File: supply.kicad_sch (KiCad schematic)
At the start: 84 parts, among them IC901 TPS7A0518PDBVT, J3 PJ-102A, Q1 BCM857BS-7-F, Q2 BCM857BS-7-F, Q3 SSM3J332R, Q4 SSM3J332R, Q901 BSS138W-7-F, Q902 BSS138W-7-F, Q903 BSS138W-7-F, SW901 PCM12SMTR, U3 TPS7B8133DRVR, U901 RB521S30T1G, U902 RB521S30T1G, U903 MP2386GG-P, U904 MP2386GG-P, U905 74LVC2G14GV, U906 74LVC1G175GV

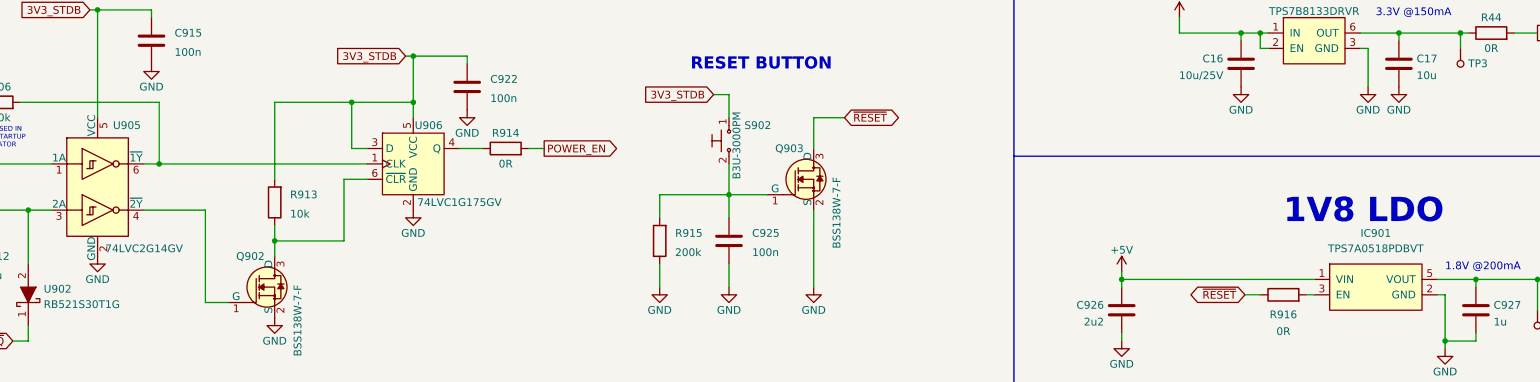
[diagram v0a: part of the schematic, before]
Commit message: SCH: Cosmetic improvement & unification
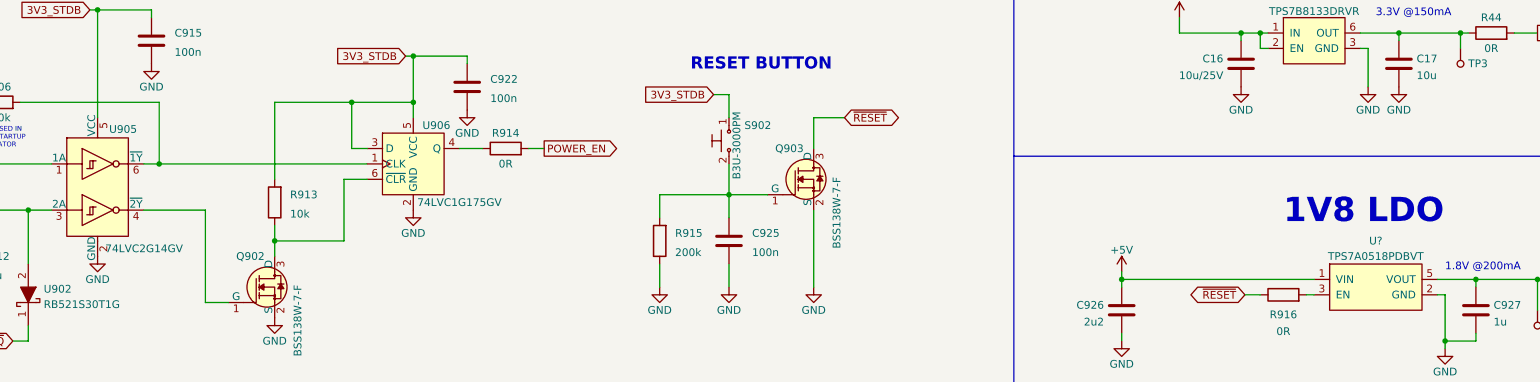
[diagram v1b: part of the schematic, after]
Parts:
- renumbered IC901 to U?
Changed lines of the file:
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@@
   (symbol (lib_id "antmicroLogicBuffersDriversReceiversTransceivers:74LVC2G14GV") (at 138.43 54.61 0) (unit 1)
     (in_bom yes) (on_board yes)
-    (property "Reference" "U905" (id 0) (at 140.97 45.72 0)
+    (property "Reference" "U905" (id 0) (at 140.335 46.355 0)
       (effects (font (size 1.27 1.27)) (justify left))
     )
@@
   (symbol (lib_id "antmicroLogicGatesandInverters:74LVC1G175GV") (at 190.5 52.07 0) (unit 1)
     (in_bom yes) (on_board yes)
-    (property "Reference" "U906" (id 0) (at 193.04 45.72 0))
+    (property "Reference" "U906" (id 0) (at 194.31 45.72 0))
     (property "Value" "74LVC1G175GV" (id 1) (at 198.12 58.42 0))
     (property "Footprint" "antmicro-footprints:SOT-23-6" (id 2) (at 190.5 69.85 0)
@@
   )
   (symbol (lib_id "antmicroPMICVoltageRegulatorsLinear:TPS7A0518PDBVT") (at 349.25 72.39 0) (unit 1)
-    (in_bom yes) (on_board yes) (fields_autoplaced)
-    (property "Reference" "IC901" (id 0) (at 349.25 63.5 0))
-    (property "Value" "TPS7A0518PDBVT" (id 1) (at 349.25 66.04 0))
+    (in_bom yes) (on_board yes)
+    (property "Reference" "U?" (id 0) (at 349.25 64.77 0))
+    (property "Value" "TPS7A0518PDBVT" (id 1) (at 349.25 67.31 0))
     (property "Footprint" "antmicro-footprints:SOT-23-5" (id 2) (at 349.25 78.74 0)
       (effects (font (size 1.27 1.27)) hide)

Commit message: Add 3V3 rail discharge
- add 3V3 rail discharge circuitry
- add 3V3 and 5V0 switch side labels
- minor improvements in arrangement on the supply sheet
- minor update on m-2 sheet
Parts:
- added Q? (x2): DMG1012T-7, antmicro-footprints:SOT-523, symbol antmicroTransistorsFETsMOSFETsSingle:DMG1012T-7
- added R?: R_100k_0402, antmicro-footprints:0402-res, symbol antmicroResistors0402:R_100k_0402
- added R?: R_5R6_0402, antmicro-footprints:0402-res, symbol antmicroResistors0402:R_5R6_0402
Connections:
- net +5V: now also R?.2
- net 3V3_EN: now also Q?.1 (G)
- net GND: now also Q?.2 (S), Q?.2 (S)
- net 3V3_SW: now reaches L902.1 (P), U904.6 (SW)
- net 3V3_SW: now also C914.2; no longer C914.1
- net 3V3_BST: now reaches U904.7 (BST)
- net 3V3_BST: now also C914.1; no longer C914.2
- net 1V8_LDO: now reaches C927.1, R45.1, TP907.1, U?.5 (VOUT)
- net 5V0_SW: now reaches C913.1, L901.1 (P), U903.6 (SW)
- net 5V0_BST: now reaches C913.2, U903.7 (BST)
- net 3V3_REG: now reaches C917.1, C919.1, C921.1, C924.1, L902.2 (P), R47.1, R911.2, TP4.1
- net 3V3_REG: now also R?.2
- net 5V0_REG: now reaches C916.1, C918.1, C920.1, C923.1, L901.2 (P), R46.1, R909.2, TP905.1
- net 3V3_LDO: now reaches C17.1, R44.1, TP3.1, U3.6 (OUT)
- new net: Q?.1 (G), Q?.3 (D), R?.1
- new net: Q?.3 (D), R?.1
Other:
- note added: "3V3 rail discharge"
- moved on the sheet: C901, C902, C904, C905, C906, C907, C908, C909, C910, C911, C913, C914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

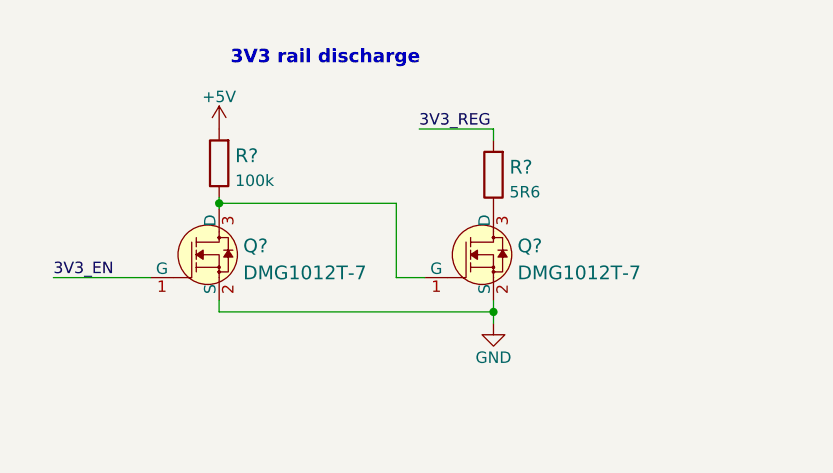
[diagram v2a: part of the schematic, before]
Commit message: Changed discharge MOSFETs to unify components used
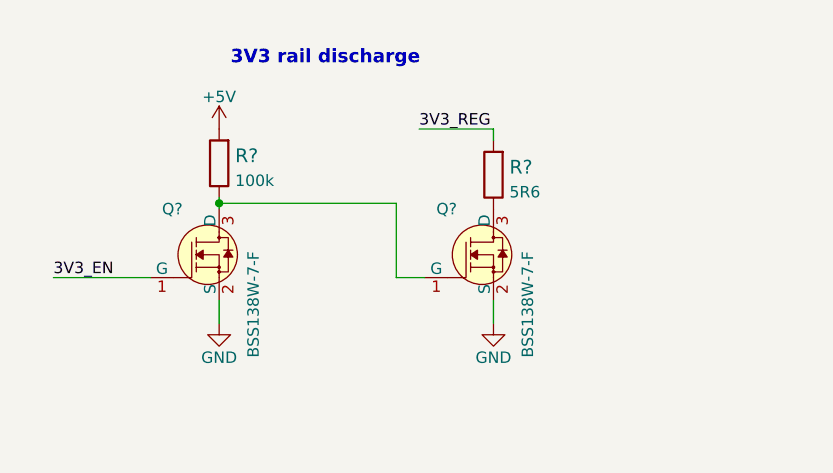
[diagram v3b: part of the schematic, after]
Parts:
- removed Q? (x2): DMG1012T-7, antmicro-footprints:SOT-523, symbol antmicroTransistorsFETsMOSFETsSingle:DMG1012T-7
- added Q? (x2): BSS138W-7-F, antmicro-footprints:SOT-323, symbol antmicroTransistorsFETsMOSFETsSingle:BSS138W-7-F
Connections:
- net 3V3_EN: now also Q?.1 (G)
- net GND: now also Q?.2 (S), Q?.2 (S)
- net at R?.1: now also Q?.1 (G), Q?.3 (D)
- net at R?.1: now also Q?.3 (D)
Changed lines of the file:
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@@
   (junction (at 353.06 127) (diameter 0) (color 0 0 0 0)
   )
-  (junction (at 279.4 267.97) (diameter 0) (color 0 0 0 0)
-  )
   (junction (at 249.555 127) (diameter 0) (color 0 0 0 0)
   )
@@
     (stroke (width 0) (type default) (color 0 0 0 0))
   )
-  (wire (pts (xy 279.4 266.7) (xy 279.4 267.97))
+  (wire (pts (xy 279.4 266.7) (xy 279.4 269.24))
     (stroke (width 0) (type default) (color 0 0 0 0))
   )
@@
     (stroke (width 0) (type default) (color 0 0 0 0))
   )
-  (wire (pts (xy 279.4 267.97) (xy 248.92 267.97))
-    (stroke (width 0) (type default) (color 0 0 0 0))
-  )
   (wire (pts (xy 339.725 127) (xy 353.06 127))
     (stroke (width 0) (type default) (color 0 0 0 0))
@@
     (stroke (width 0) (type default) (color 0 0 0 0))
   )
-  (wire (pts (xy 248.92 267.97) (xy 248.92 266.7))
-    (stroke (width 0) (type default) (color 0 0 0 0))
-  )
   (wire (pts (xy 374.015 208.28) (xy 374.015 209.55))
     (stroke (width 0) (type default) (color 0 0 0 0))
@@
     (stroke (width 0) (type default) (color 0 0 0 0))
   )
-  (wire (pts (xy 279.4 267.97) (xy 279.4 269.24))
-    (stroke (width 0) (type default) (color 0 0 0 0))
-  )
   (polyline (pts (xy 12.7 252.73) (xy 219.075 252.73))
     (stroke (width 0) (type default) (color 0 0 0 0))
@@
     (stroke (width 0) (type default) (color 0 0 0 0))
   )
+  (wire (pts (xy 248.92 266.7) (xy 248.92 269.24))
+    (stroke (width 0) (type default) (color 0 0 0 0))
+  )
   (wire (pts (xy 50.8 52.07) (xy 50.8 66.04))
     (stroke (width 0) (type default) (color 0 0 0 0))
@@
     (pin "1")
   )
-  (symbol (lib_id "antmicroTransistorsFETsMOSFETsSingle:DMG1012T-7") (at 248.92 261.62 0) (unit 1)
-    (in_bom yes) (on_board yes) (fields_autoplaced)
-    (property "Reference" "Q?" (id 0) (at 251.587 260.6438 0)
-      (effects (font (size 1.524 1.524)) (justify left))
-    )
-    (property "Value" "DMG1012T-7" (id 1) (at 251.587 263.6372 0)
-      (effects (font (size 1.524 1.524)) (justify left))
-    )
-    (property "Footprint" "antmicro-footprints:SOT-523" (id 2) (at 254 256.54 0)
-      (effects (font (size 1.524 1.524)) (justify left) hide)
-    )
-    (property "Datasheet" "https://www.diodes.com/assets/Datasheets/ds31783.pdf" (id 3) (at 254 254 0)
-      (effects (font (size 1.524 1.524)) (justify left) hide)
-    )
-    (property "MPN" "DMG1012T-7" (id 4) (at 254 248.92 0)
-      (effects (font (size 1.524 1.524)) (justify left) hide)
-    )
-    (property "Manufacturer" "Diodes Incorporated" (id 5) (at 254 233.68 0)
-      (effects (font (size 1.524 1.524)) (justify left) hide)
-    )
-    (pin "1")
-    (pin "2")
-    (pin "3")
-  )
   (symbol (lib_id "antmicroResistors0402:R_40k2_1%_0402") (at 340.36 200.66 90) (unit 1)
     (in_bom yes) (on_board yes) (fields_autoplaced)
@@
     (pin "2")
   )
+  (symbol (lib_id "power:GND") (at 248.92 269.24 0) (unit 1)
+    (in_bom yes) (on_board yes)
+    (property "Reference" "#PWR?" (id 0) (at 248.92 275.59 0)
+      (effects (font (size 1.27 1.27)) hide)
+    )
+    (property "Value" "GND" (id 1) (at 248.92 273.05 0))
+    (property "Footprint" "" (id 2) (at 248.92 269.24 0)
+      (effects (font (size 1.27 1.27)) hide)
+    )
+    (property "Datasheet" "" (id 3) (at 248.92 269.24 0)
+      (effects (font (size 1.27 1.27)) hide)
+    )
+    (pin "1")
+  )
   (symbol (lib_id "antmicroCapacitors0402:C_10u_0402") (at 116.84 68.58 0) (unit 1)
     (in_bom yes) (on_board yes)
@@
     (pin "1")
   )
+  (symbol (lib_id "antmicroTransistorsFETsMOSFETsSingle:BSS138W-7-F") (at 279.4 261.62 0) (unit 1)
+    (in_bom yes) (on_board yes)
+    (property "Reference" "Q?" (id 0) (at 273.05 256.54 0)
+      (effects (font (size 1.27 1.27)) (justify left))
+    )
+    (property "Value" "BSS138W-7-F" (id 1) (at 283.21 273.05 90)
+      (effects (font (size 1.27 1.27)) (justify left))
+    )
+    (property "Footprint" "antmicro-footprints:SOT-323" (id 2) (at 284.48 256.54 0)
+      (effects (font (size 1.524 1.524)) (justify left) hide)
+    )
+    (property "Datasheet" "https://www.diodes.com/assets/Datasheets/BSS138W.pdf" (id 3) (at 284.48 254 0)
+      (effects (font (size 1.524 1.524)) (justify left) hide)
+    )
+    (property "MPN" "BSS138W-7-F" (id 4) (at 284.48 248.92 0)
+      (effects (font (size 1.524 1.524)) (justify left) hide)
+    )
+    (property "Manufacturer" "Diodes Incorporated" (id 5) (at 284.48 233.68 0)
+      (effects (font (size 1.524 1.524)) (justify left) hide)
+    )
+    (pin "1")
+    (pin "2")
+    (pin "3")
+  )
   (symbol (lib_id "power:GND") (at 58.42 154.94 0) (unit 1)
     (in_bom yes) (on_board yes)
@@
     (pin "1")
   )
+  (symbol (lib_id "antmicroTransistorsFETsMOSFETsSingle:BSS138W-7-F") (at 248.92 261.62 0) (unit 1)
+    (in_bom yes) (on_board yes)
+    (property "Reference" "Q?" (id 0) (at 242.57 256.54 0)
+      (effects (font (size 1.27 1.27)) (justify left))
+    )
+    (property "Value" "BSS138W-7-F" (id 1) (at 252.73 273.05 90)
+      (effects (font (size 1.27 1.27)) (justify left))
+    )
+    (property "Footprint" "antmicro-footprints:SOT-323" (id 2) (at 254 256.54 0)
+      (effects (font (size 1.524 1.524)) (justify left) hide)
+    )
+    (property "Datasheet" "https://www.diodes.com/assets/Datasheets/BSS138W.pdf" (id 3) (at 254 254 0)
+      (effects (font (size 1.524 1.524)) (justify left) hide)
+    )
+    (property "MPN" "BSS138W-7-F" (id 4) (at 254 248.92 0)
+      (effects (font (size 1.524 1.524)) (justify left) hide)
+    )
+    (property "Manufacturer" "Diodes Incorporated" (id 5) (at 254 233.68 0)
+      (effects (font (size 1.524 1.524)) (justify left) hide)
+    )
+    (pin "1")
+    (pin "2")
+    (pin "3")
+  )
   (symbol (lib_id "power:GND") (at 116.84 72.39 0) (unit 1)
     (in_bom yes) (on_board yes)
@@
     (pin "1")
   )
-  (symbol (lib_id "antmicroTransistorsFETsMOSFETsSingle:DMG1012T-7") (at 279.4 261.62 0) (unit 1)
-    (in_bom yes) (on_board yes) (fields_autoplaced)
-    (property "Reference" "Q?" (id 0) (at 282.067 260.6438 0)
-      (effects (font (size 1.524 1.524)) (justify left))
-    )
-    (property "Value" "DMG1012T-7" (id 1) (at 282.067 263.6372 0)
-      (effects (font (size 1.524 1.524)) (justify left))
-    )
-    (property "Footprint" "antmicro-footprints:SOT-523" (id 2) (at 284.48 256.54 0)
-      (effects (font (size 1.524 1.524)) (justify left) hide)
-    )
-    (property "Datasheet" "https://www.diodes.com/assets/Datasheets/ds31783.pdf" (id 3) (at 284.48 254 0)
-      (effects (font (size 1.524 1.524)) (justify left) hide)
-    )
-    (property "MPN" "DMG1012T-7" (id 4) (at 284.48 248.92 0)
-      (effects (font (size 1.524 1.524)) (justify left) hide)
-    )
-    (property "Manufacturer" "Diodes Incorporated" (id 5) (at 284.48 233.68 0)
-      (effects (font (size 1.524 1.524)) (justify left) hide)
-    )
-    (pin "1")
-    (pin "2")
-    (pin "3")
-  )
   (symbol (lib_id "power:GND") (at 340.36 212.09 0) (unit 1)

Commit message: Reannotate parts
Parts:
- gave numbers to parts that had none: 5
- renumbered C903 to C116, C912 to C117, C915 to C118, C922 to C119, C901 to C120, C902 to C121, C904 to C122, C905 to C123, C925 to C124, C906 to C125, C907 to C126, C908 to C127, C909 to C128, C910 to C129, C911 to C130, C926 to C131, C913 to C132, C914 to C133, C16 to C134, C916 to C135, C917 to C136, C17 to C137, C918 to C138, C919 to C139, C920 to C140, C921 to C141, C927 to C142, C923 to C143, C924 to C144, J3 to J12, L901 to L1, L902 to L2, Q901 to Q12, Q1 to Q13, Q2 to Q14, Q3 to Q15, Q4 to Q16, Q902 to Q17, Q903 to Q19, R901 to R249, R38 to R250, R39 to R251, R40 to R252, R41 to R253, R42 to R254, R43 to R255, R902 to R256, R903 to R257, R906 to R258, R913 to R259, R914 to R260, R915 to R261, R904 to R263, R905 to R264, R907 to R266, R908 to R267, R916 to R268, R909 to R269, R910 to R270, R911 to R271, R912 to R272, R44 to R273, R46 to R274, R47 to R275, R45 to R276, S901 to S4, S902 to S5, SW901 to SW1, TP901 to TP48, TP902 to TP49, TP903 to TP50, TP904 to TP51, TP3 to TP52, TP905 to TP53, TP4 to TP54, TP907 to TP55, U901 to U35, U902 to U36, U905 to U37, U906 to U38, U903 to U39, U904 to U40, U3 to U41

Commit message: Added protection diodes to supply sheet
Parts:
- added D? (x2): DF2S30FS, antmicro-footprints:SOD-923, symbol antmicroTVSDiodes:DF2S30FS
- added D? (x4): ESD9X5.0ST5G, antmicro-footprints:SOD-923, symbol antmicroTVSDiodes:ESD9X5.0ST5G
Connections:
- net +1V8: now also D?.1
- net +3V3: now also D?.1
- net +5V: now also D?.1; no longer R262.2
- net 3V3_STDB: now also R262.2, D?.1
- net GND: now also D?.2, D?.2, D?.2, D?.2, D?.2, D?.2
- net VCC: now also D?.1
- net at J12.1, Q13.4, Q15.3 (D): now also D?.1

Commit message: Annotate parts
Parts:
- gave numbers to parts that had none: 6
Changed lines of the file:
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@@
   (symbol (lib_id "antmicroTVSDiodes:DF2S30FS") (at 44.45 138.43 90) (unit 1)
     (in_bom yes) (on_board yes) (fields_autoplaced)
-    (property "Reference" "D?" (id 0) (at 41.275 136.8188 90)
+    (property "Reference" "D28" (id 0) (at 41.275 136.8188 90)
       (effects (font (size 1.27 1.27)) (justify left))
     )
@@
   (symbol (lib_id "antmicroTVSDiodes:ESD9X5.0ST5G") (at 389.89 76.2 90) (unit 1)
     (in_bom yes) (on_board yes)
-    (property "Reference" "D?" (id 0) (at 392.43 77.47 90)
+    (property "Reference" "D31" (id 0) (at 392.43 77.47 90)
       (effects (font (size 1.27 1.27)) (justify right))
     )
@@
   (symbol (lib_id "power:GND") (at 44.45 142.24 0) (mirror y) (unit 1)
     (in_bom yes) (on_board yes) (fields_autoplaced)
-    (property "Reference" "#PWR?" (id 0) (at 44.45 148.59 0)
+    (property "Reference" "#PWR0312" (id 0) (at 44.45 148.59 0)
       (effects (font (size 1.27 1.27)) hide)
     )
@@
   (symbol (lib_id "power:GND") (at 373.38 40.64 0) (mirror y) (unit 1)
     (in_bom yes) (on_board yes)
-    (property "Reference" "#PWR?" (id 0) (at 373.38 46.99 0)
+    (property "Reference" "#PWR0310" (id 0) (at 373.38 46.99 0)
       (effects (font (size 1.27 1.27)) hide)
     )
@@
   (symbol (lib_id "power:GND") (at 389.89 207.01 0) (mirror y) (unit 1)
     (in_bom yes) (on_board yes)
-    (property "Reference" "#PWR?" (id 0) (at 389.89 213.36 0)
+    (property "Reference" "#PWR0270" (id 0) (at 389.89 213.36 0)
       (effects (font (size 1.27 1.27)) hide)
     )
@@
   (symbol (lib_id "power:GND") (at 105.41 224.79 0) (mirror y) (unit 1)
     (in_bom yes) (on_board yes) (fields_autoplaced)
-    (property "Reference" "#PWR?" (id 0) (at 105.41 231.14 0)
+    (property "Reference" "#PWR0311" (id 0) (at 105.41 231.14 0)
       (effects (font (size 1.27 1.27)) hide)
     )
@@
   (symbol (lib_id "antmicroTVSDiodes:ESD9X5.0ST5G") (at 389.89 203.2 90) (unit 1)
     (in_bom yes) (on_board yes)
-    (property "Reference" "D?" (id 0) (at 392.43 204.47 90)
+    (property "Reference" "D33" (id 0) (at 392.43 204.47 90)
       (effects (font (size 1.27 1.27)) (justify right))
     )
@@
   (symbol (lib_id "power:GND") (at 389.89 135.89 0) (mirror y) (unit 1)
     (in_bom yes) (on_board yes)
-    (property "Reference" "#PWR?" (id 0) (at 389.89 142.24 0)
+    (property "Reference" "#PWR0309" (id 0) (at 389.89 142.24 0)
       (effects (font (size 1.27 1.27)) hide)
     )
@@
   (symbol (lib_id "antmicroTVSDiodes:ESD9X5.0ST5G") (at 373.38 36.83 90) (unit 1)
     (in_bom yes) (on_board yes)
-    (property "Reference" "D?" (id 0) (at 375.92 38.1 90)
+    (property "Reference" "D30" (id 0) (at 375.92 38.1 90)
       (effects (font (size 1.27 1.27)) (justify right))
     )
@@
   (symbol (lib_id "antmicroTVSDiodes:DF2S30FS") (at 105.41 220.98 90) (unit 1)
     (in_bom yes) (on_board yes) (fields_autoplaced)
-    (property "Reference" "D?" (id 0) (at 102.235 219.3688 90)
+    (property "Reference" "D29" (id 0) (at 102.235 219.3688 90)
       (effects (font (size 1.27 1.27)) (justify left))
     )
@@
   (symbol (lib_id "power:GND") (at 389.89 80.01 0) (mirror y) (unit 1)
     (in_bom yes) (on_board yes)
-    (property "Reference" "#PWR?" (id 0) (at 389.89 86.36 0)
+    (property "Reference" "#PWR0143" (id 0) (at 389.89 86.36 0)
       (effects (font (size 1.27 1.27)) hide)
     )
@@
   (symbol (lib_id "antmicroTVSDiodes:ESD9X5.0ST5G") (at 389.89 132.08 90) (unit 1)
     (in_bom yes) (on_board yes)
-    (property "Reference" "D?" (id 0) (at 392.43 133.35 90)
-      (effects (font (size 1.27 1.27)) (justify right))
-    )
+    (property "Reference" "D32" (id 0) (at 392.43 133.35 90)
+      (effects (font (size 1.27 1.27)) (justify right))
+    )
